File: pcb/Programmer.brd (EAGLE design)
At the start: 38.1 x 26 mm, 47 parts, among them J1 MINI-USB-JACK, U1 TPD4S012DRYR, U10 SN74LV1T126DCKR, U2 FT232HQ, U3 SN74LV1T125DCKR, U4 SN74LV1T125DCKR, U5 SN74LV1T125DCKR, U6 SN74LV1T125DCKR, U7 SN74LV1T125DCKR, U8 SN74LV1T125DCKR, U9 SN74LV1T126DCKR, X1 SIT8021

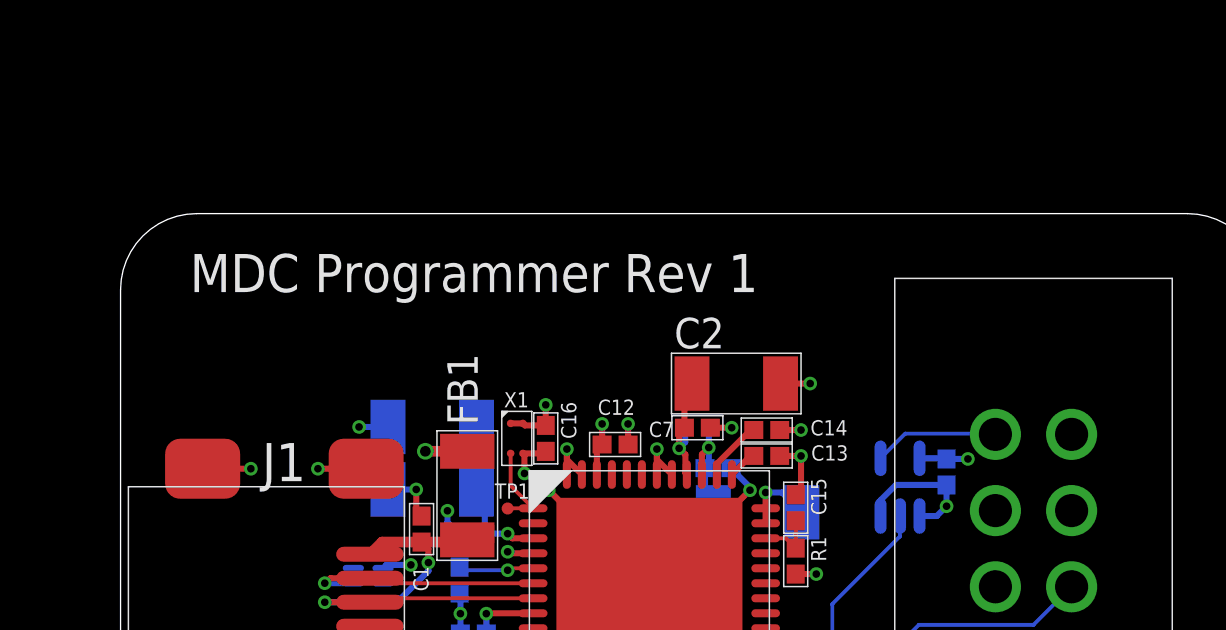
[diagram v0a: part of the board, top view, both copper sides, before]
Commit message: Update part numbers
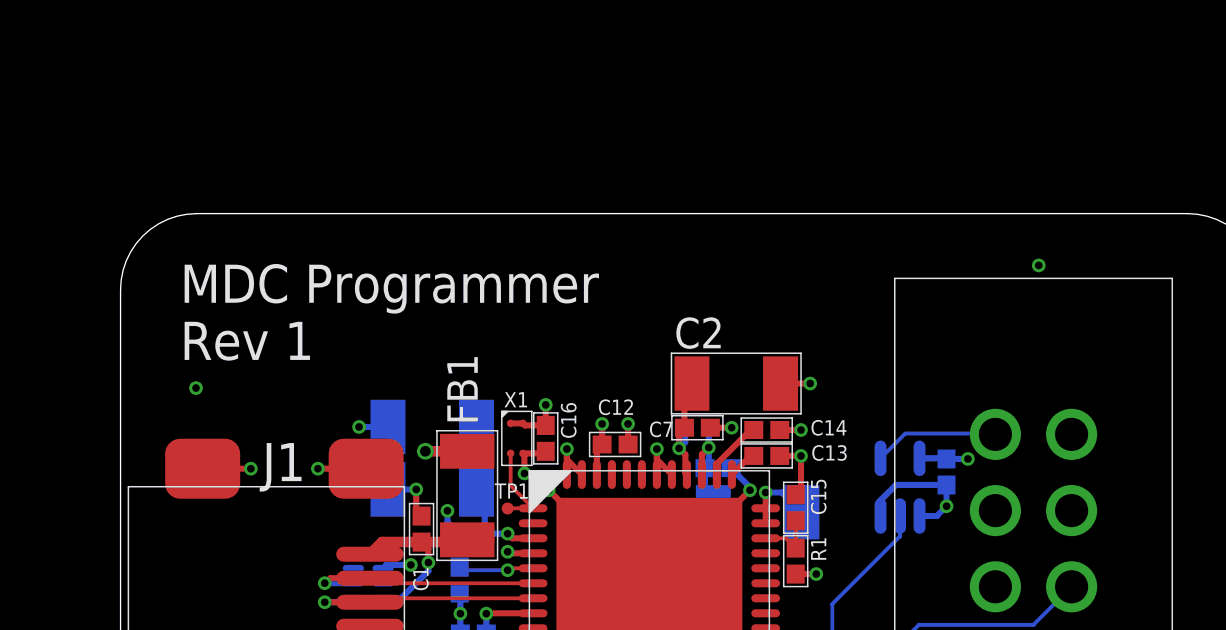
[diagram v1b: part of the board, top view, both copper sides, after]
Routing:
- net GND: vias 36 -> 38
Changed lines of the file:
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@@
 <layer number="14" name="Route14" color="22" fill="1" visible="no" active="no"/>
 <layer number="15" name="Power" color="23" fill="1" visible="no" active="yes"/>
-<layer number="16" name="Bottom" color="1" fill="1" visible="no" active="yes"/>
+<layer number="16" name="Bottom" color="1" fill="1" visible="yes" active="yes"/>
 <layer number="17" name="Pads" color="2" fill="1" visible="yes" active="yes"/>
 <layer number="18" name="Vias" color="2" fill="1" visible="yes" active="yes"/>
@@
 <layer number="20" name="Dimension" color="24" fill="1" visible="yes" active="yes"/>
 <layer number="21" name="tPlace" color="7" fill="1" visible="yes" active="yes"/>
-<layer number="22" name="bPlace" color="7" fill="1" visible="no" active="yes"/>
+<layer number="22" name="bPlace" color="7" fill="1" visible="yes" active="yes"/>
 <layer number="23" name="tOrigins" color="15" fill="1" visible="yes" active="yes"/>
-<layer number="24" name="bOrigins" color="15" fill="1" visible="no" active="yes"/>
+<layer number="24" name="bOrigins" color="15" fill="1" visible="yes" active="yes"/>
 <layer number="25" name="tNames" color="7" fill="1" visible="yes" active="yes"/>
-<layer number="26" name="bNames" color="7" fill="1" visible="no" active="yes"/>
+<layer number="26" name="bNames" color="7" fill="1" visible="yes" active="yes"/>
 <layer number="27" name="tValues" color="7" fill="1" visible="yes" active="yes"/>
-<layer number="28" name="bValues" color="7" fill="1" visible="no" active="yes"/>
+<layer number="28" name="bValues" color="7" fill="1" visible="yes" active="yes"/>
 <layer number="29" name="tStop" color="7" fill="3" visible="yes" active="yes"/>
-<layer number="30" name="bStop" color="7" fill="6" visible="no" active="yes"/>
-<layer number="31" name="tCream" color="7" fill="4" visible="yes" active="yes"/>
+<layer number="30" name="bStop" color="7" fill="6" visible="yes" active="yes"/>
+<layer number="31" name="tCream" color="7" fill="4" visible="no" active="yes"/>
 <layer number="32" name="bCream" color="7" fill="5" visible="no" active="yes"/>
-<layer number="33" name="tFinish" color="6" fill="3" visible="yes" active="yes"/>
+<layer number="33" name="tFinish" color="6" fill="3" visible="no" active="yes"/>
 <layer number="34" name="bFinish" color="6" fill="6" visible="no" active="yes"/>
-<layer number="35" name="tGlue" color="7" fill="4" visible="yes" active="yes"/>
+<layer number="35" name="tGlue" color="7" fill="4" visible="no" active="yes"/>
 <layer number="36" name="bGlue" color="7" fill="5" visible="no" active="yes"/>
-<layer number="37" name="tTest" color="7" fill="1" visible="yes" active="yes"/>
+<layer number="37" name="tTest" color="7" fill="1" visible="no" active="yes"/>
 <layer number="38" name="bTest" color="7" fill="1" visible="no" active="yes"/>
 <layer number="39" name="tKeepout" color="4" fill="11" visible="no" active="yes"/>
 <layer number="40" name="bKeepout" color="1" fill="11" visible="no" active="yes"/>
 <layer number="41" name="tRestrict" color="4" fill="10" visible="yes" active="yes"/>
-<layer number="42" name="bRestrict" color="1" fill="10" visible="no" active="yes"/>
-<layer number="43" name="vRestrict" color="2" fill="10" visible="no" active="yes"/>
+<layer number="42" name="bRestrict" color="1" fill="10" visible="yes" active="yes"/>
+<layer number="43" name="vRestrict" color="2" fill="10" visible="yes" active="yes"/>
 <layer number="44" name="Drills" color="7" fill="1" visible="no" active="yes"/>
 <layer number="45" name="Holes" color="7" fill="1" visible="no" active="yes"/>
@@
 <wire x1="35.56" y1="26.035" x2="2.54" y2="26.035" width="0" layer="20"/>
 <wire x1="2.54" y1="26.035" x2="0" y2="23.495" width="0" layer="20" curve="90"/>
-<text x="2.3114" y="23.4188" size="1.27" layer="25" font="vector" ratio="10">MDC Programmer Rev 1</text>
+<text x="1.9812" y="21.1582" size="1.27" layer="25" font="vector" ratio="10">MDC Programmer
+Rev 1</text>
 <text x="1.9558" y="0.762" size="0.635" layer="25" font="vector" ratio="10">GND</text>
 <text x="4.699" y="0.762" size="0.635" layer="25" font="vector" ratio="10">ICE40_TX</text>
@@
 <attribute name="MFG" value="FTDI" x="35.4076" y="5.842" size="1.778" layer="27" display="off"/>
 <attribute name="NAME" x="22.3266" y="10.5789" size="1.016" layer="25" font="vector"/>
-<attribute name="PN" value="FT232HQ" x="35.4076" y="5.842" size="1.778" layer="27" display="off"/>
+<attribute name="PN" value="FT232HQ-REEL" x="35.4076" y="5.842" size="1.778" layer="27" display="off"/>
 </element>
 <element name="X1" library="EagleLibrary" package="SIT8021" value="SIT8021" x="13.208" y="18.542" smashed="yes">
@@
 <vertex x="46.1518" y="47.5658625"/>
 </polygon>
+<via x="2.5146" y="20.2184" extent="1-16" drill="0.254"/>
+<via x="30.607" y="24.3078" extent="1-16" drill="0.254"/>
 </signal>
 <signal name="1V8">
@@
 </drawing>
 <compatibility>
+<note version="6.3" minversion="6.2.2" severity="warning">
+Since Version 6.2.2 text objects can contain more than one line,
+which will not be processed correctly with this version.
+</note>
 <note version="8.3" severity="warning">
 Since Version 8.3, EAGLE supports URNs for individual library
